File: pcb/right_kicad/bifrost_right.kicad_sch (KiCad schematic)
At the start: 64 parts, among them J1 HRO_TYPE-C-31-M-12, J2 Conn_01x02, J3 Conn_01x06, J4 Conn_01x05, Q1 AO3401A, Q2 2N7002, Q3 AO3401A, SW1 SW_Push, SW10 SW_Push, SW11 SW_Push, SW12 SW_Push, SW13 SW_Push, SW14 SW_Push, SW15 SW_Push, SW16 SW_Push, SW17 SW_Push, SW18 SW_Push, SW19 SW_Push, SW2 SW_Push, SW20 SW_Push, SW21 SW_Push, SW22 SW_Push, SW23 SW_Push, SW3 SW_Push, SW4 SW_Push, SW5 SW_Push, SW6 SW_Push, SW7 SW_Push, SW8 SW_Push, SW9 SW_Push, T1 TS24CA, U1 MDBT50Q-1MV2, U2 TP4057, U3 SRV05-4, X1 32.768kHz

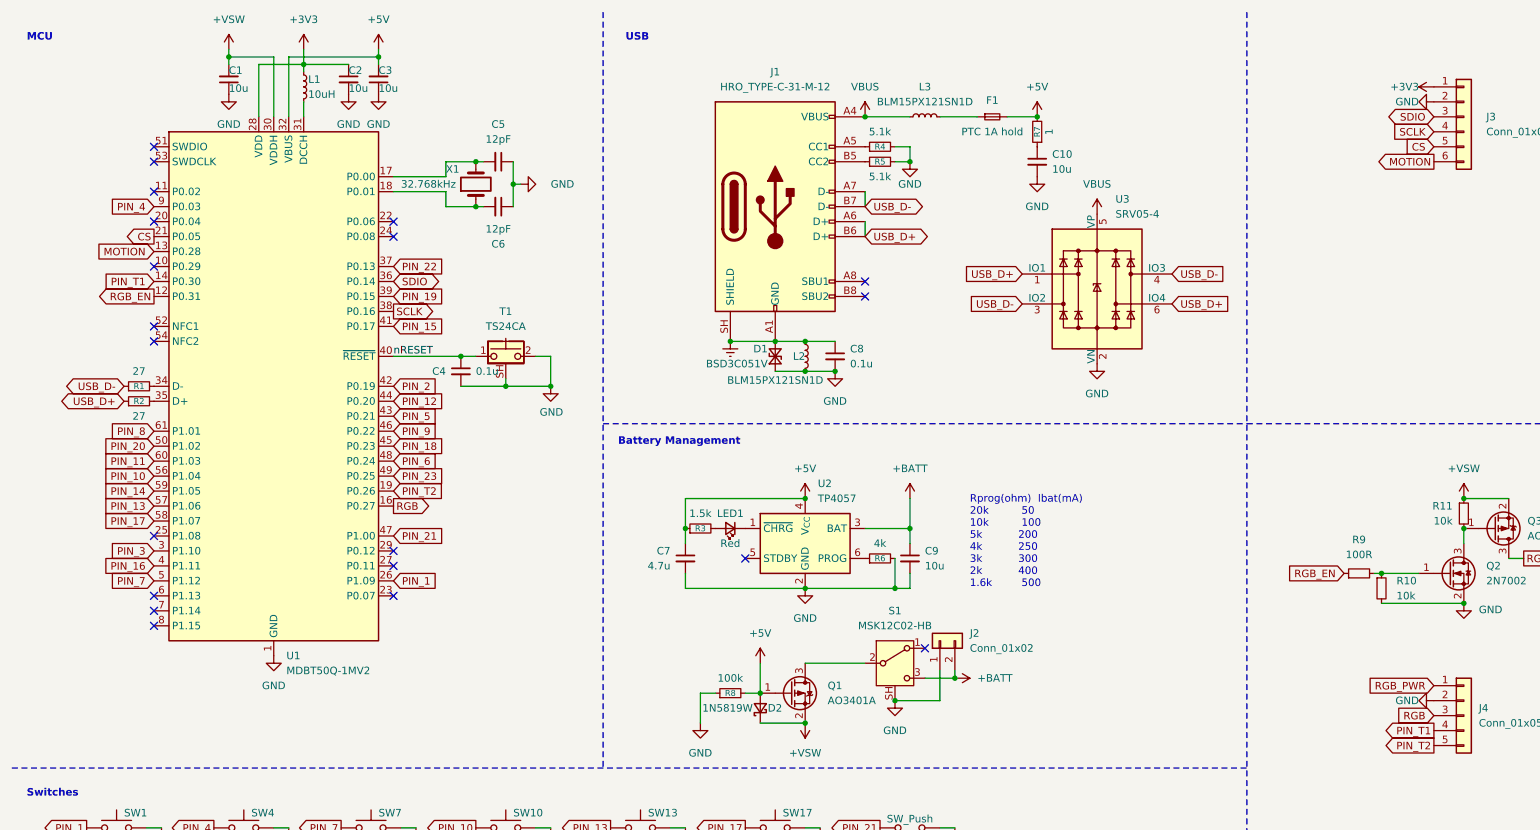
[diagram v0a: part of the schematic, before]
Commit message: Update KiCad keyboard designs
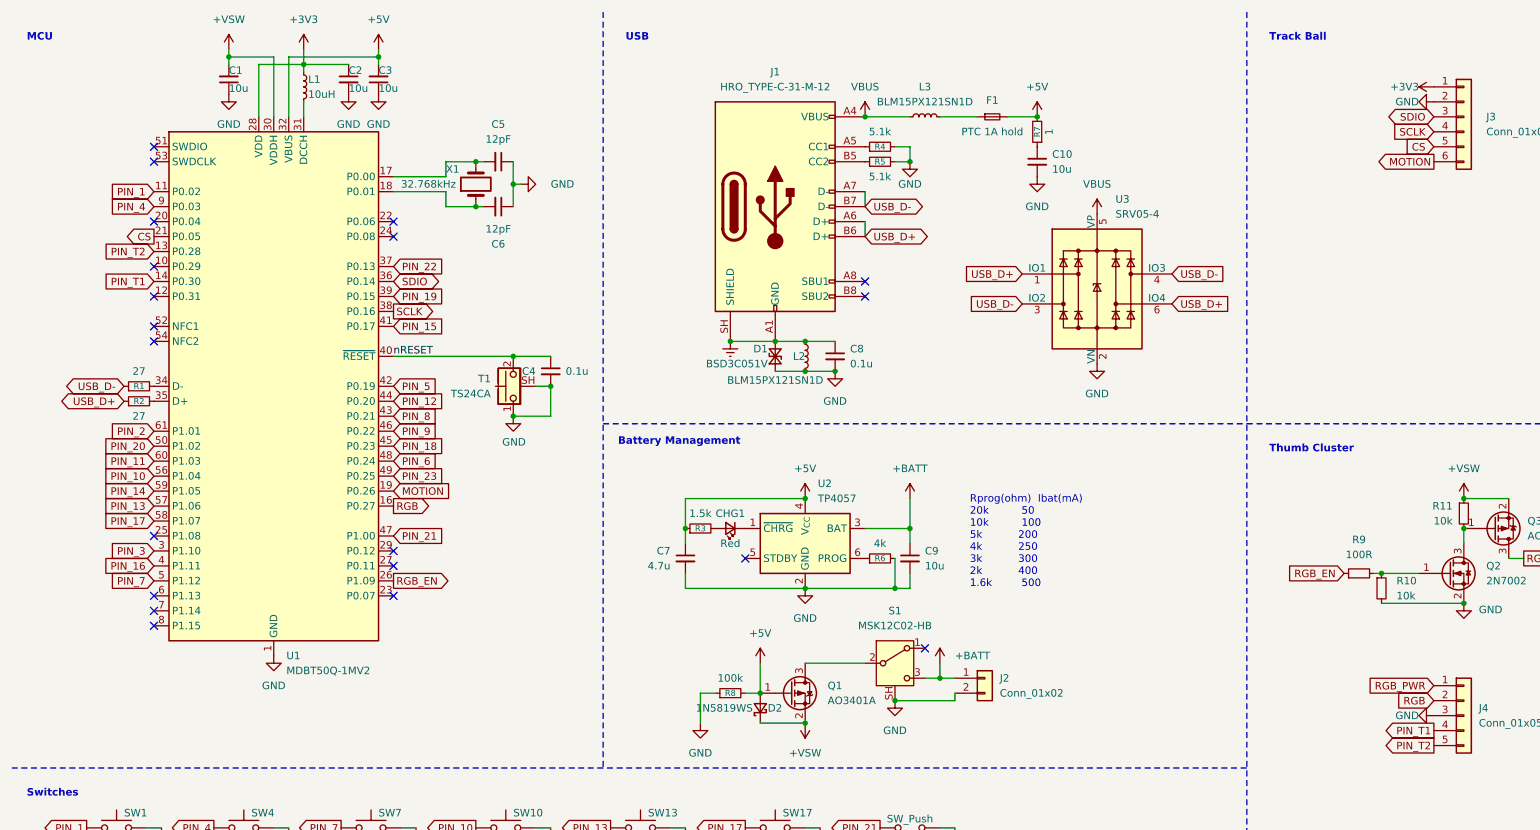
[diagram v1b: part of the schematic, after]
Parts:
- D2: value 1N5819W -> 1N5819WS; footprint Diode_SMD:D_SOD-123 -> Diode_SMD:D_SOD-323
- J2: footprint Connector_Molex:Molex_PicoBlade_53398-0271_1x02-1MP_P1.25mm_Vertical -> Connector_PinHeader_1.27mm:PinHeader_1x02_P1.27mm_Vertical
- J3: footprint Connector_PinHeader_2.54mm:PinHeader_1x06_P2.54mm_Vertical -> Connector_PinHeader_1.27mm:PinHeader_1x06_P1.27mm_Vertical
- J4: footprint Connector_PinHeader_2.54mm:PinHeader_1x05_P2.54mm_Vertical -> Connector_PinHeader_1.27mm:PinHeader_1x05_P1.27mm_Vertical
- renumbered LED1 to CHG1
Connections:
- net +BATT: now also J2.1 (Pin_1); no longer J2.2 (Pin_2)
- net GND: now also J2.2 (Pin_2), J4.3 (Pin_3), T1.1; no longer J2.1 (Pin_1), J4.2 (Pin_2), T1.2
- net MOTION: now also U1.19 (P0.26); no longer U1.13 (P0.28)
- net PIN_1: now also U1.11 (P0.02); no longer U1.26 (P1.09)
- net PIN_2: now also U1.61 (P1.01); no longer U1.42 (P0.19)
- net PIN_5: now also U1.42 (P0.19); no longer U1.43 (P0.21)
- net PIN_8: now also U1.43 (P0.21); no longer U1.61 (P1.01)
- net PIN_T2: now also U1.13 (P0.28); no longer U1.19 (P0.26)
- net RGB: now also J4.2 (Pin_2); no longer J4.3 (Pin_3)
- net RGB_EN: now also U1.26 (P1.09); no longer U1.12 (P0.31)
- net nRESET: now also T1.2; no longer T1.1
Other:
- note added: "Thumb Cluster"
- note added: "Track Ball"
- moved on the sheet: C4, J2, T1

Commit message: Update PCB designs
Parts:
- SW1, SW10, SW11, SW12, SW13, SW14, SW15, SW16, SW17, SW19, SW2, SW20, SW22, SW23, SW3, SW4, SW5, SW6, SW7, SW8, SW9: value SW_Push -> 1U
- SW18: value SW_Push -> 2.25U
- SW21: value SW_Push -> 1.5U
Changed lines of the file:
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@@
 			)
 		)
-		(property "Value" "SW_Push"
+		(property "Value" "2.25U"
 			(at 142.24 165.354 0)
 			(show_name no)
@@
 			)
 		)
-		(property "Value" "SW_Push"
+		(property "Value" "1.5U"
 			(at 165.1 149.606 0)
 			(show_name no)
@@
 			)
 		)
-		(property "Value" "SW_Push"
+		(property "Value" "1U"
 			(at 119.38 187.706 0)
 			(show_name no)
@@
 			)
 		)
-		(property "Value" "SW_Push"
+		(property "Value" "1U"
 			(at 142.24 152.654 0)
 			(show_name no)
@@
 			)
 		)
-		(property "Value" "SW_Push"
+		(property "Value" "1U"
 			(at 165.1 178.054 0)
 			(show_name no)
@@
 			)
 		)
-		(property "Value" "SW_Push"
+		(property "Value" "1U"
 			(at 142.24 178.054 0)
 			(show_name no)
@@
 			)
 		)
-		(property "Value" "SW_Push"
+		(property "Value" "1U"
 			(at 165.1 187.706 0)
 			(show_name no)
@@
 			)
 		)
-		(property "Value" "SW_Push"
+		(property "Value" "1U"
 			(at 142.24 187.706 0)
 			(show_name no)
@@
 			)
 		)
-		(property "Value" "SW_Push"
+		(property "Value" "1U"
 			(at 52.07 152.654 0)
 			(show_name no)
@@
 			)
 		)
-		(property "Value" "SW_Push"
+		(property "Value" "1U"
 			(at 73.66 152.654 0)
 			(show_name no)
@@
 			)
 		)
-		(property "Value" "SW_Push"
+		(property "Value" "1U"
 			(at 52.07 178.054 0)
 			(show_name no)
@@
 			)
 		)
-		(property "Value" "SW_Push"
+		(property "Value" "1U"
 			(at 96.52 152.654 0)
 			(show_name no)
@@
 			)
 		)
-		(property "Value" "SW_Push"
+		(property "Value" "1U"
 			(at 73.66 178.054 0)
 			(show_name no)
@@
 			)
 		)
-		(property "Value" "SW_Push"
+		(property "Value" "1U"
 			(at 119.38 152.654 0)
 			(show_name no)
@@
 			)
 		)
-		(property "Value" "SW_Push"
+		(property "Value" "1U"
 			(at 30.48 152.654 0)
 			(show_name no)
@@
 			)
 		)
-		(property "Value" "SW_Push"
+		(property "Value" "1U"
 			(at 30.48 178.054 0)
 			(show_name no)
@@
 			)
 		)
-		(property "Value" "SW_Push"
+		(property "Value" "1U"
 			(at 119.38 165.354 0)
 			(show_name no)
@@
 			)
 		)
-		(property "Value" "SW_Push"
+		(property "Value" "1U"
 			(at 96.52 165.354 0)
 			(show_name no)
@@
 			)
 		)
-		(property "Value" "SW_Push"
+		(property "Value" "1U"
 			(at 96.52 178.054 0)
 			(show_name no)
@@
 			)
 		)
-		(property "Value" "SW_Push"
+		(property "Value" "1U"
 			(at 119.38 178.054 0)
 			(show_name no)
@@
 			)
 		)
-		(property "Value" "SW_Push"
+		(property "Value" "1U"
 			(at 30.48 165.354 0)
 			(show_name no)
@@
 			)
 		)
-		(property "Value" "SW_Push"
+		(property "Value" "1U"
 			(at 73.66 165.354 0)
 			(show_name no)
@@
 			)
 		)
-		(property "Value" "SW_Push"
+		(property "Value" "1U"
 			(at 52.07 165.354 0)
 			(show_name no)

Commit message: Update PCB designs
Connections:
- net CS: no longer J3.5 (Pin_5)
- new net nCS: J3.5 (Pin_5)
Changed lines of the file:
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@@
 		)
 	)
-	(global_label "CS"
+	(global_label "nCS"
 		(shape input)
 		(at 254 35.56 180)
@@
 		)
 		(property "Intersheetrefs" "${INTERSHEET_REFS}"
-			(at 248.5353 35.56 0)
+			(at 247.3863 35.56 0)
 			(hide yes)
 			(show_name no)

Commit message: Update PCB BOM and manufacturing outputs
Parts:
- removed C10: 10u, Capacitor_SMD:C_0402_1005Metric, symbol Device:C_Small
- removed R7: 1, Resistor_SMD:R_0402_1005Metric, symbol Device:R_Small
- C1, C2, C3, C9: JLCPCB Part # (none) -> C15525
- C4: renamed from C5; JLCPCB Part # (none) -> C1547
- C5: renamed from C6; JLCPCB Part # (none) -> C1547
- C6: renamed from C4; value 0.1u -> 100n; JLCPCB Part # (none) -> C1525
- C7: JLCPCB Part # (none) -> C23733
- C8: value 0.1u -> 100n; JLCPCB Part # (none) -> C1525
- CHG1: JLCPCB Part # (none) -> C19189741
- D1: JLCPCB Part # (none) -> C151996
- D2: JLCPCB Part # (none) -> C191023
- F1: JLCPCB Part # (none) -> C883131
- J1: JLCPCB Part # (none) -> C51911914
- J2, J3, J4, SW1, SW10, SW11, SW12, SW13, SW14, SW15, SW16, SW17, SW18, SW19, SW2, SW20, SW21, SW22, SW23, SW3, SW4, SW5, SW6, SW7, SW8, SW9: now left out of the parts list
- L1: footprint Inductor_SMD:L_0402_1005Metric -> Inductor_SMD:L_0603_1608Metric; JLCPCB Part # (none) -> C86083
- L2, L3: JLCPCB Part # (none) -> C88970
- Q1, Q3: JLCPCB Part # (none) -> C15127
- Q2: JLCPCB Part # (none) -> C8545
- R1, R2: JLCPCB Part # (none) -> C25100
- R10: renamed from R11; JLCPCB Part # (none) -> C25744
- R3: JLCPCB Part # (none) -> C25867
- R4: renamed from R8; JLCPCB Part # (none) -> C25741
- R5: renamed from R4; JLCPCB Part # (none) -> C25905
- R6: renamed from R5; JLCPCB Part # (none) -> C25905
- R7: renamed from R6; value 4k -> 3.3k; JLCPCB Part # (none) -> C25890
- R8: renamed from R9; value 100R -> 100; JLCPCB Part # (none) -> C25076
- R9: renamed from R10; JLCPCB Part # (none) -> C25744
- S1: JLCPCB Part # (none) -> C431541
- T1: JLCPCB Part # (none) -> C393942
- U1: JLCPCB Part # (none) -> C5118826
- U2: JLCPCB Part # (none) -> C12044
- U3: JLCPCB Part # (none) -> C7420376
- X1: JLCPCB Part # (none) -> C32346
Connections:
- net CS is gone; now on net nCS: U1.21 (P0.05)
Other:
- moved on the sheet: D2, J2, Q1, R4, S1

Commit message: Publish current main PCB manufacturing data
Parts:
- J1: JLCPCB Part # C51911914 -> C165948
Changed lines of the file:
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@@
 			)
 		)
-		(property "JLCPCB Part #" "C51911914"
+		(property "JLCPCB Part #" "C165948"
 			(at 142.24 45.72 0)
 			(hide yes)

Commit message: Refactor application implementation
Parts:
- U2: footprint Package_TO_SOT_SMD:TSOT-23-6 -> Package_TO_SOT_SMD:SOT-23-6
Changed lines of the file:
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@@
 			)
 		)
-		(property "Footprint" "Package_TO_SOT_SMD:TSOT-23-6"
+		(property "Footprint" "Package_TO_SOT_SMD:SOT-23-6"
 			(at 147.32 115.57 0)
 			(hide yes)

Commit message: Update Bifrost case and PCB outputs
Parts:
- added TP1: SWDIO, TestPoint:TestPoint_THTPad_D1.0mm_Drill0.5mm, symbol Connector:TestPoint_Small
- added TP2: SWDCLK, TestPoint:TestPoint_THTPad_D1.0mm_Drill0.5mm, symbol Connector:TestPoint_Small
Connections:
- net GND: now also J4.2 (Pin_2); no longer J4.3 (Pin_3)
- net RGB: now also J4.3 (Pin_3); no longer J4.2 (Pin_2)
- net at U1.51 (SWDIO): now also TP1.1
- net at U1.53 (SWDCLK): now also TP2.1
- no-connect marks 21 -> 19
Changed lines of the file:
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@@
 	)
 	(no_connect
-		(at 36.83 38.1)
-	)
-	(no_connect
-		(at 36.83 35.56)
-	)
-	(no_connect
 		(at 170.18 120.65)
 	)
@@
 	(global_label "RGB"
 		(shape input)
-		(at 254 129.54 180)
+		(at 254 132.08 180)
 		(fields_autoplaced yes)
 		(effects
@@
 		)
 		(property "Intersheetrefs" "${INTERSHEET_REFS}"
-			(at 247.2048 129.54 0)
+			(at 247.2048 132.08 0)
 			(hide yes)
 			(show_name no)
@@
 	)
 	(symbol
+		(lib_id "Connector:TestPoint_Small")
+		(at 36.83 35.56 180)
+		(unit 1)
+		(body_style 1)
+		(exclude_from_sim no)
+		(in_bom yes)
+		(on_board yes)
+		(in_pos_files yes)
+		(dnp no)
+		(property "Reference" "TP1"
+			(at 35.56 33.782 0)
+			(show_name no)
+			(do_not_autoplace no)
+			(effects
+				(font
+					(size 1.27 1.27)
+				)
+				(justify left)
+			)
+		)
+		(property "Value" "SWDIO"
+			(at 35.56 35.56 0)
+			(show_name no)
+			(do_not_autoplace no)
+			(effects
+				(font
+					(size 1.27 1.27)
+				)
+				(justify left)
+			)
+		)
+		(property "Footprint" "TestPoint:TestPoint_THTPad_D1.0mm_Drill0.5mm"
+			(at 31.75 35.56 0)
+			(hide yes)
+			(show_name no)
+			(do_not_autoplace no)
+			(effects
+				(font
+					(size 1.27 1.27)
+				)
+			)
+		)
+		(property "Datasheet" ""
+			(at 31.75 35.56 0)
+			(hide yes)
+			(show_name no)
+			(do_not_autoplace no)
+			(effects
+				(font
+					(size 1.27 1.27)
+				)
+			)
+		)
+		(property "Description" "test point"
+			(at 36.83 35.56 0)
+			(hide yes)
+			(show_name no)
+			(do_not_autoplace no)
+			(effects
+				(font
+					(size 1.27 1.27)
+				)
+			)
+		)
+		(pin "1"
+		)
+		(instances
+			(project "bifrost_right"
+				(path "/e7e89169-ab7b-68cd-1b0e-3f8776099a22"
+					(reference "TP1")
+					(unit 1)
+				)
+			)
+		)
+	)
+	(symbol
 		(lib_id "Device:C_Small")
 		(at 69.85 24.13 0)
@@
 	)
 	(symbol
+		(lib_id "Connector:TestPoint_Small")
+		(at 36.83 38.1 0)
+		(unit 1)
+		(body_style 1)
+		(exclude_from_sim no)
+		(in_bom yes)
+		(on_board yes)
+		(in_pos_files yes)
+		(dnp no)
+		(property "Reference" "TP2"
+			(at 35.56 38.1 0)
+			(show_name no)
+			(do_not_autoplace no)
+			(effects
+				(font
+					(size 1.27 1.27)
+				)
+				(justify right)
+			)
+		)
+		(property "Value" "SWDCLK"
+			(at 35.56 39.878 0)
+			(show_name no)
+			(do_not_autoplace no)
+			(effects
+				(font
+					(size 1.27 1.27)
+				)
+				(justify right)
+			)
+		)
+		(property "Footprint" "TestPoint:TestPoint_THTPad_D1.0mm_Drill0.5mm"
+			(at 41.91 38.1 0)
+			(hide yes)
+			(show_name no)
+			(do_not_autoplace no)
+			(effects
+				(font
+					(size 1.27 1.27)
+				)
+			)
+		)
+		(property "Datasheet" ""
+			(at 41.91 38.1 0)
+			(hide yes)
+			(show_name no)
+			(do_not_autoplace no)
+			(effects
+				(font
+					(size 1.27 1.27)
+				)
+			)
+		)
+		(property "Description" "test point"
+			(at 36.83 38.1 0)
+			(hide yes)
+			(show_name no)
+			(do_not_autoplace no)
+			(effects
+				(font
+					(size 1.27 1.27)
+				)
+			)
+		)
+		(pin "1"
+		)
+		(instances
+			(project "bifrost_right"
+				(path "/e7e89169-ab7b-68cd-1b0e-3f8776099a22"
+					(reference "TP2")
+					(unit 1)
+				)
+			)
+		)
+	)
+	(symbol
 		(lib_id "Device:C_Small")
 		(at 49.53 24.13 180)
@@
 		(lib_name "GND_12")
 		(lib_id "power:GND")
-		(at 254 132.08 270)
+		(at 254 129.54 270)
 		(unit 1)
 		(body_style 1)
@@
 		(fields_autoplaced yes)
 		(property "Reference" "#PWR050"
-			(at 247.65 132.08 0)
+			(at 247.65 129.54 0)
 			(hide yes)
 			(show_name no)
@@
 		)
 		(property "Value" "GND"
-			(at 251.46 132.0799 90)
+			(at 251.46 129.5399 90)
 			(show_name no)
 			(do_not_autoplace no)
@@
 		)
 		(property "Footprint" ""
-			(at 254 132.08 0)
+			(at 254 129.54 0)
 			(hide yes)
 			(show_name no)
@@
 		)
 		(property "Datasheet" ""
-			(at 254 132.08 0)
+			(at 254 129.54 0)
 			(hide yes)
 			(show_name no)
@@
 		)
 		(property "Description" "Power symbol creates a global label with name \"GND\" , ground"
-			(at 254 132.08 0)
+			(at 254 129.54 0)
 			(hide yes)
 			(show_name no)

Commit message: Update PCB designs and production files
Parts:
- R3: value 1.5k -> 1k; JLCPCB Part # C25867 -> C11702
- X1: JLCPCB Part # C32346 -> C479190
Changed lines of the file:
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@@
 			)
 		)
-		(property "JLCPCB Part #" "C32346"
+		(property "JLCPCB Part #" "C479190"
 			(at 91.44 41.91 90)
 			(hide yes)
@@
 			)
 		)
-		(property "Value" "1.5k"
+		(property "Value" "1k"
 			(at 129.54 97.79 90)
 			(show_name no)
@@
 			)
 		)
-		(property "JLCPCB Part #" "C25867"
+		(property "JLCPCB Part #" "C11702"
 			(at 129.54 100.33 90)
 			(hide yes)
